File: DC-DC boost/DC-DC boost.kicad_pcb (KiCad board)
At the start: 2 copper layers, 17 x 14 mm, 7 parts, among them J1 Conn_01x03, U1 TPS63030DSK

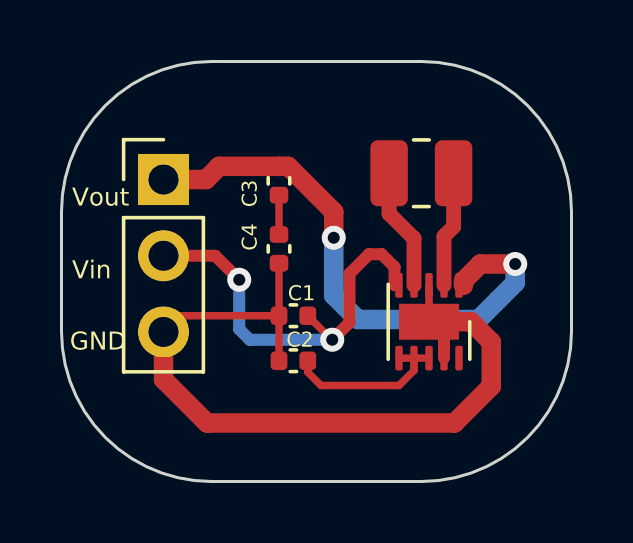
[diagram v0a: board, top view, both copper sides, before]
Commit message: change the layout of the 3.3v-out module
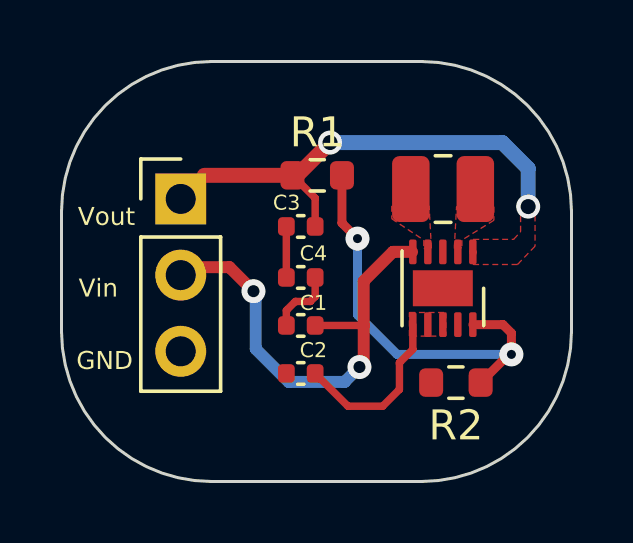
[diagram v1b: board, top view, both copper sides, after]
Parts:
- added R1: 2.8M, Resistor_SMD:R_0603_1608Metric, F.Cu at (123.5, 83.8)
- added R2: 500K, Resistor_SMD:R_0603_1608Metric, F.Cu at (128.1, 90.7)
- moved C3 1.69 mm to (123.0, 85.5), turned to 180 degrees
- moved U1 1.21 mm to (127.7, 87.6)
- moved C4 1.20 mm to (123.0, 87.2), turned to 0 degrees
- moved FTC252012S1R5MBCA1 0.90 mm to (127.7, 84.3)
- moved J1 0.86 mm to (119.0, 84.6)
- moved C2 0.49 mm to (123.0, 90.4)
- moved C1 0.41 mm to (123.0, 88.8)
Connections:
- U1 pad 10: Net-(J1-Pin_1) -> Net-(U1-FB)
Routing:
- net Net-(J1-Pin_3): track 27.4 -> 2.29 mm
- net Net-(U1-FB): track 0.00 -> 14.1 mm, vias 0 -> 2
- net Net-(U1-L1): track 4.08 -> 0.00 mm
- net Net-(U1-L2): track 3.87 -> 0.00 mm
- net Net-(J1-Pin_1): track 18.9 -> 16.4 mm
- net Net-(J1-Pin_2): track 13.9 -> 15.5 mm
- added copper zone on F.Cu, net Net-(J1-Pin_1)
- added copper zone on F.Cu, net Net-(J1-Pin_3)
- added copper zone on F.Cu, net Net-(U1-EN)
- added copper zone on F.Cu, net Net-(U1-L1)
- added copper zone on F.Cu, net Net-(U1-L2)
